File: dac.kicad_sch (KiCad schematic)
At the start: 10 parts, among them U11 TL074CDT, U12 MCP4728-E_UN

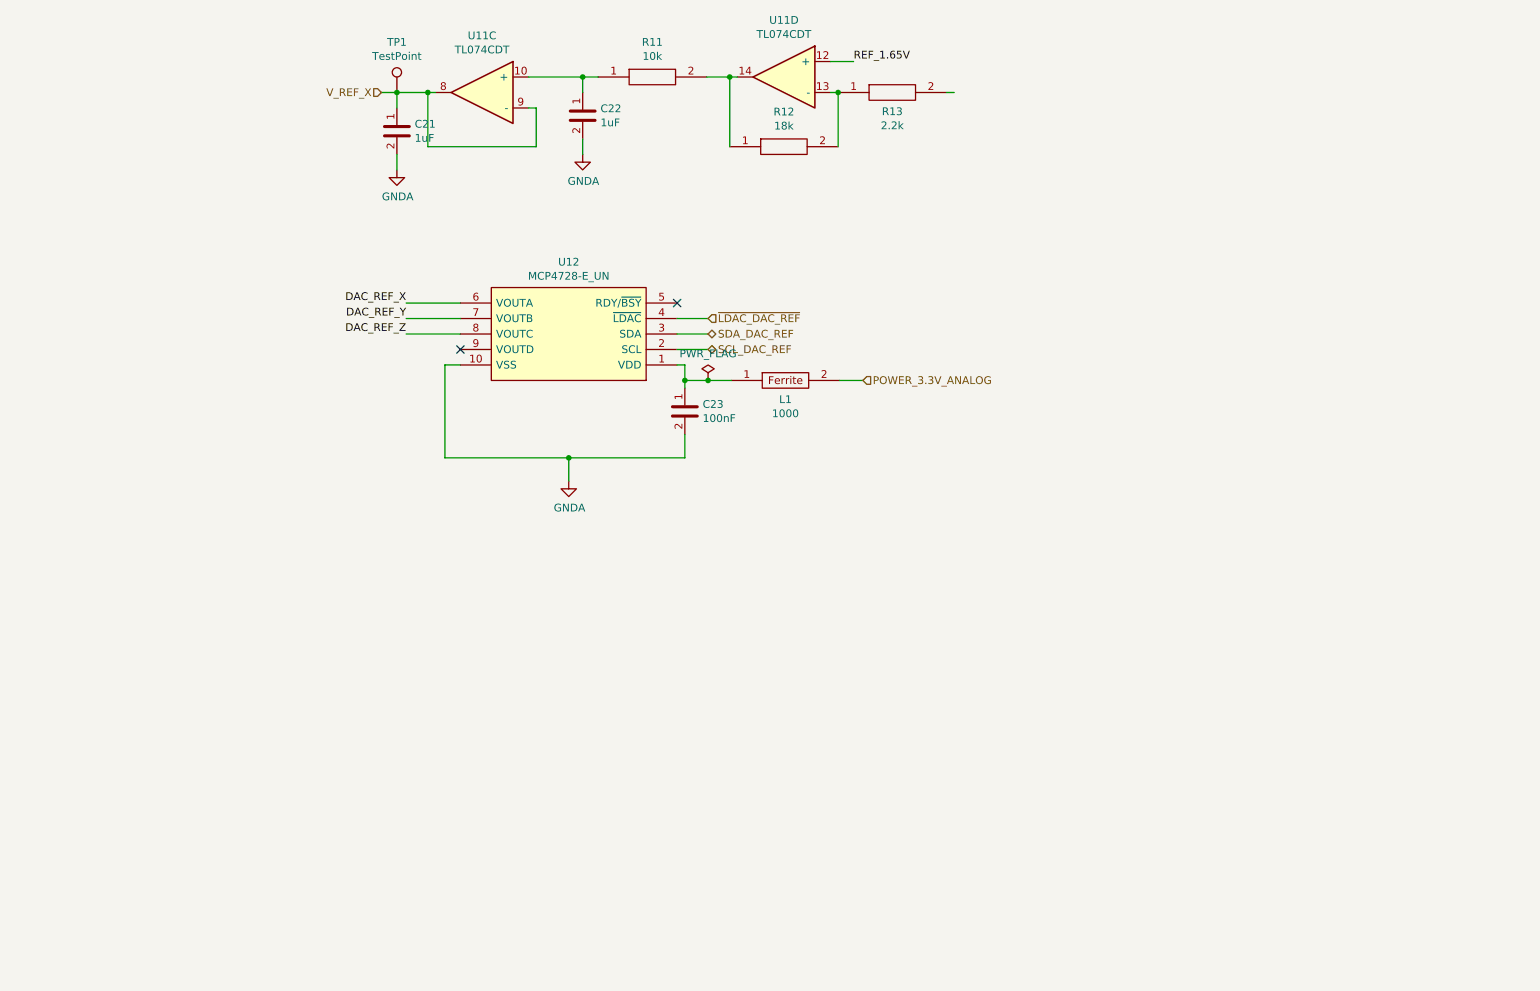
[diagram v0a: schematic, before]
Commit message: Added DAC circuit.
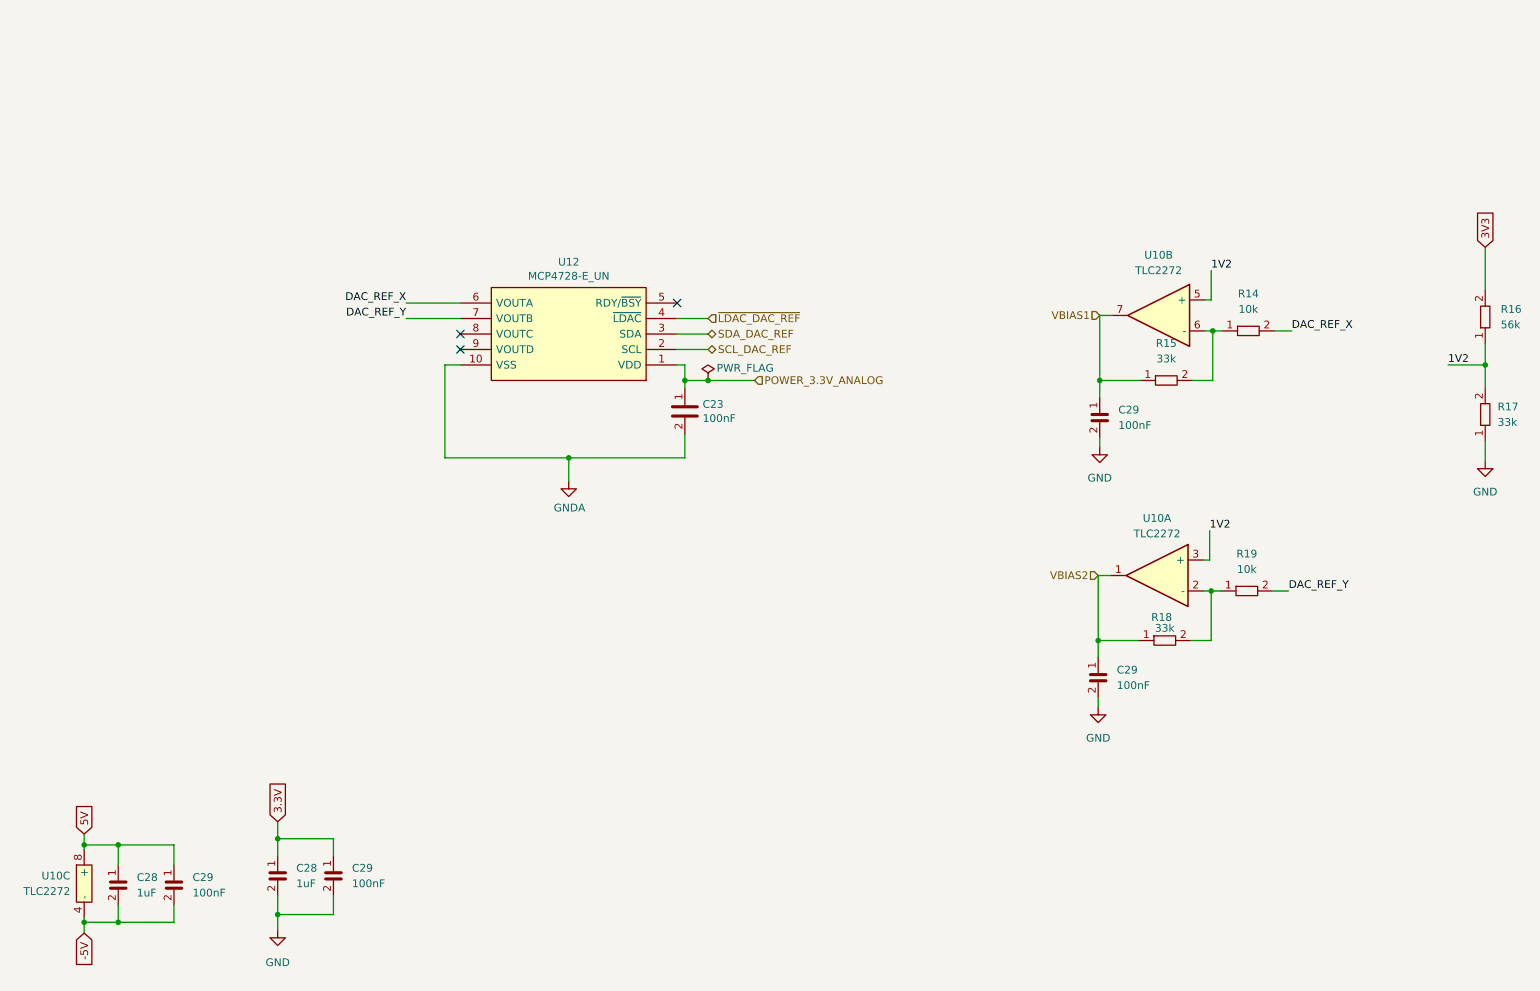
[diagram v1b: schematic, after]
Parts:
- removed C21, C22: C0603_1uF_25V, Capacitor_SMD:C_0603_1608Metric, symbol Basis_Platine_Kompass-rescue:C0603_1uF_25V-Jojo_Kicad_Lib
- removed L1: L0603_Ferrite_Bead_1k, Resistor_SMD:R_0603_1608Metric, symbol Basis_Platine_Kompass-rescue:L0603_Ferrite_Bead_1k-Jojo_Kicad_Lib
- removed R11: R0603_10k, Resistor_SMD:R_0603_1608Metric, symbol Basis_Platine_Kompass-rescue:R0603_10k-Jojo_Kicad_Lib
- removed R12: R0603_18k, Resistor_SMD:R_0603_1608Metric, symbol Basis_Platine_Kompass-rescue:R0603_18k-Jojo_Kicad_Lib
- removed R13: R0603_2.2k, Resistor_SMD:R_0603_1608Metric, symbol Basis_Platine_Kompass-rescue:R0603_2.2k-Jojo_Kicad_Lib
- removed TP1: TestPoint, TestPoint:TestPoint_Pad_D1.5mm, symbol Basis_Platine_Kompass-rescue:TestPoint-Jojo_Kicad_Lib
- removed U11: TL074CDT, SamacSys_Parts:SOIC127P600X175-14N, symbol Basis_Platine_Kompass-rescue:TL074CDT-Jojo_Kicad_Lib
- added C28 (x2): C0402_1uF_6.3V, Capacitor_SMD:C_0402_1005Metric, symbol Jojos_Lib:C0402_1uF_6.3V
- added C29 (x4): C0402_100nF_50V, Capacitor_SMD:C_0402_1005Metric, symbol Jojos_Lib:C0402_100nF_50V
- added R14, R19: R0402_10k, Resistor_SMD:R_0402_1005Metric, symbol Jojos_Lib:R0402_10k
- added R15, R17, R18: R0402_33k, Resistor_SMD:R_0402_1005Metric, symbol Jojos_Lib:R0402_33k
- added R16: R0402_56k, Resistor_SMD:R_0402_1005Metric, symbol Jojos_Lib:R0402_56k
- added U10: TLC2272, Package_SO:SO-8_3.9x4.9mm_P1.27mm, symbol Jojos_Lib:TLC2272CD
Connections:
- net DAC_REF_X: now also R14.2
- net DAC_REF_Y: now also R19.2
- net POWER_3.3V_ANALOG: now also C23.1, U12.1 (VDD)
- net DAC_REF_Z: no longer names the net of U12.8 (VOUTC)
- new net: R14.1, R15.2, U10.6 (-)
- new net: R18.2, R19.1, U10.2 (-)
- new net -5V: C28.2, C29.2, U10.4 (-)
- new net 1V2: R16.1, R17.2, U10.3 (+), U10.5 (+)
- new net 3.3V: C28.1, C29.1
- new net 3V3: R16.2
- new net 5V: C28.1, C29.1, U10.8 (+)
- new net GND: C28.2, C29.2, C29.2, C29.2, R17.1
- new net VBIAS1: C29.1, R15.1, U10.7
- new net VBIAS2: C29.1, R18.1, U10.1
- no-connect marks 2 -> 3

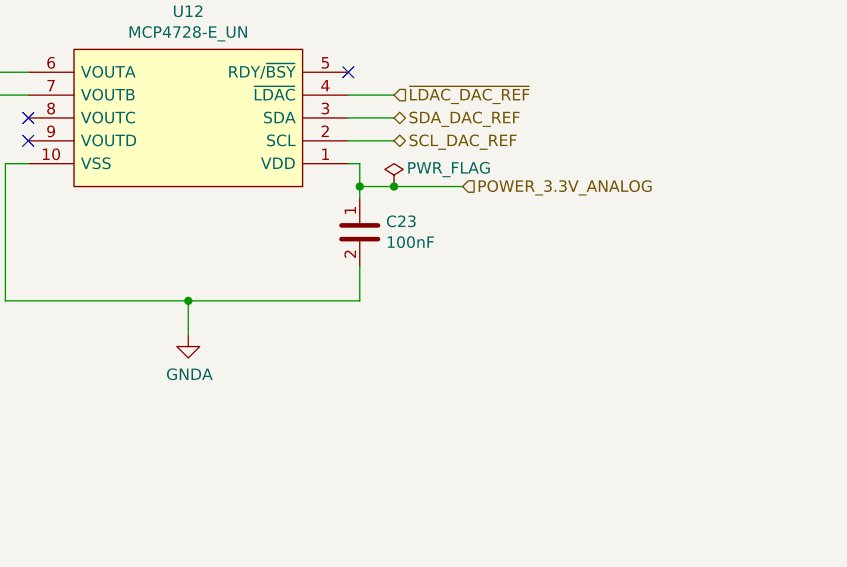
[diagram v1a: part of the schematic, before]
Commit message: Changed power supply.
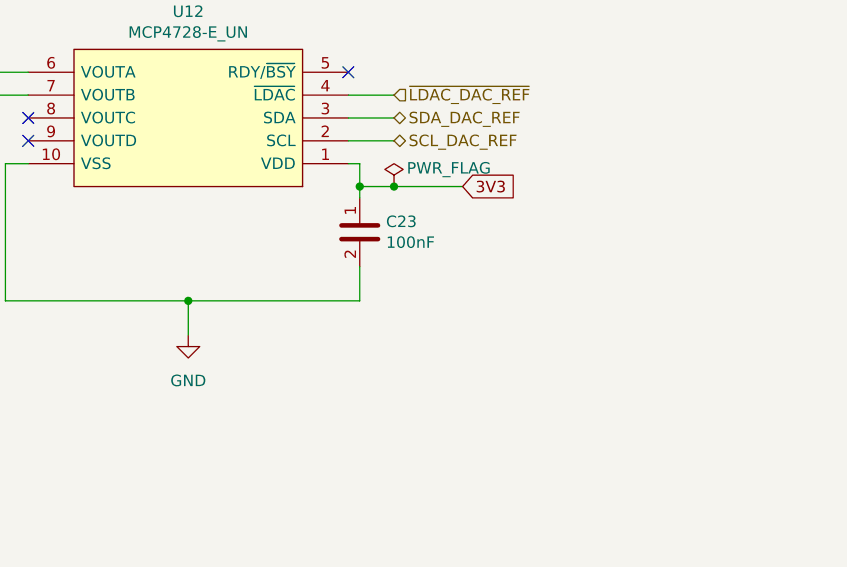
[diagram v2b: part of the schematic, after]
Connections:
- net GNDA is gone; now on net GND: C23.2, U12.10 (VSS)
- net POWER_3.3V_ANALOG is gone; now on net 3V3: C23.1, U12.1 (VDD)
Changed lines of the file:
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@@
+    )
+  )
+  (global_label "3V3" (shape input) (at 135.382 95.504 0) (fields_autoplaced)
+    (effects (font (size 1.27 1.27)) (justify left))
+    (property "Intersheetrefs" "${INTERSHEET_REFS}" (at 141.7954 95.504 0)
+      (effects (font (size 1.27 1.27)) (justify left) hide)
     )
   )
@@
   (hierarchical_label "VBIAS1" (shape input) (at 192.024 84.836 180) (fields_autoplaced)
     (effects (font (size 1.27 1.27)) (justify right))
-  )
-  (hierarchical_label "POWER_3.3V_ANALOG" (shape input) (at 135.382 95.504 0) (fields_autoplaced)
-    (effects (font (size 1.27 1.27)) (justify left))
   )
   (hierarchical_label "SDA_DAC_REF" (shape bidirectional) (at 127.762 87.884 0) (fields_autoplaced)
@@
     )
   )
-  (symbol (lib_id "power:GNDA") (at 104.902 112.014 0) (unit 1)
-    (in_bom yes) (on_board yes) (dnp no)
-    (property "Reference" "#PWR021" (at 104.902 118.364 0)
-      (effects (font (size 1.27 1.27)) hide)
-    )
-    (property "Value" "GNDA" (at 105.029 116.4082 0)
-      (effects (font (size 1.27 1.27)))
-    )
-    (property "Footprint" "" (at 104.902 112.014 0)
-      (effects (font (size 1.27 1.27)) hide)
-    )
-    (property "Datasheet" "" (at 104.902 112.014 0)
-      (effects (font (size 1.27 1.27)) hide)
-    )
-    (pin "1")
-    (instances
-      (project "CMEX"
-        (path "/03c4a148-37f4-4d5a-ada3-efb0d725ba7b"
-          (reference "#PWR021") (unit 1)
-        )
-        (path "/03c4a148-37f4-4d5a-ada3-efb0d725ba7b/4e3d1fe0-3870-440f-98d4-103735aef720"
-          (reference "#PWR020") (unit 1)
-        )
-      )
-      (project "Basis_Platine_Kompass"
-        (path "/8966b6e5-9901-4983-a621-a9b0fedaa794/00000000-0000-0000-0000-00005eadd7ff"
-          (reference "#PWR035") (unit 1)
-        )
-      )
-    )
-  )
   (symbol (lib_id "Jojos_Lib:TLC2272CD") (at 24.638 177.8 0) (unit 3)
     (in_bom yes) (on_board yes) (dnp no) (fields_autoplaced)
@@
         )
       )
+    )
+  )
+  (symbol (lib_id "power:GND") (at 104.902 112.014 0) (unit 1)
+    (in_bom yes) (on_board yes) (dnp no) (fields_autoplaced)
+    (property "Reference" "#PWR019" (at 104.902 118.364 0)
+      (effects (font (size 1.27 1.27)) hide)
+    )
+    (property "Value" "GND" (at 104.902 117.094 0)
+      (effects (font (size 1.27 1.27)))
+    )
+    (property "Footprint" "" (at 104.902 112.014 0)
+      (effects (font (size 1.27 1.27)) hide)
+    )
+    (property "Datasheet" "" (at 104.902 112.014 0)
+      (effects (font (size 1.27 1.27)) hide)
+    )
+    (pin "1")
+    (instances
+      (project "CMEX"
+        (path "/03c4a148-37f4-4d5a-ada3-efb0d725ba7b/4e3d1fe0-3870-440f-98d4-103735aef720"
+          (reference "#PWR019") (unit 1)
+        )
+      )

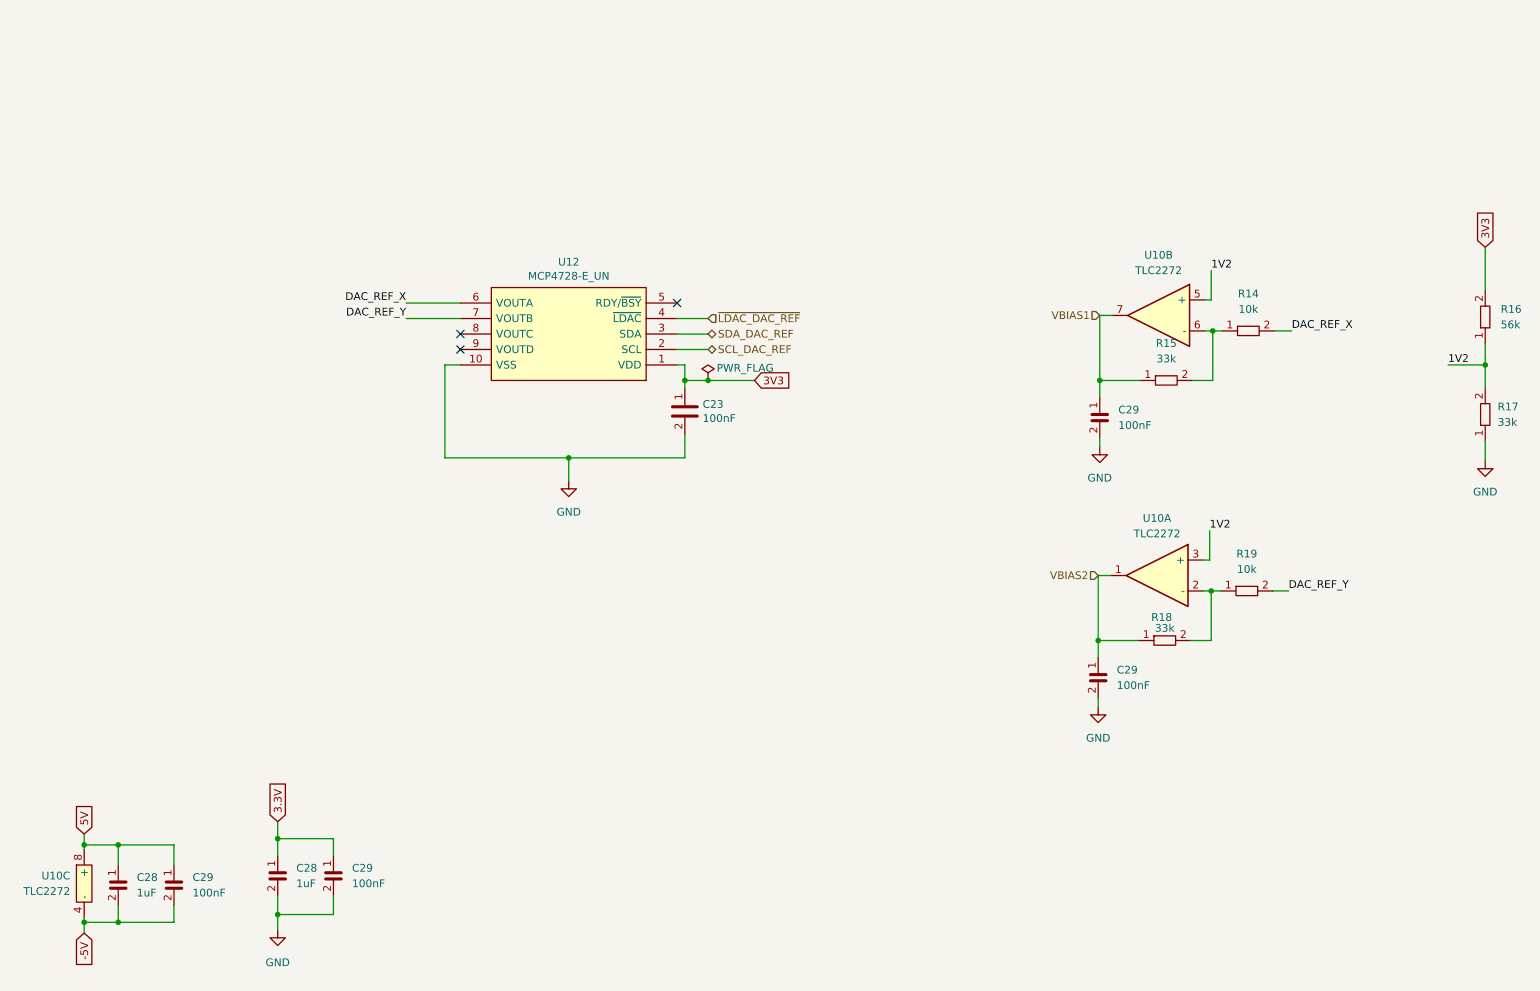
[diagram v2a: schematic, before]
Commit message: Changed global to hierarchichal lables, reorganized main sheet to get pins to connector.
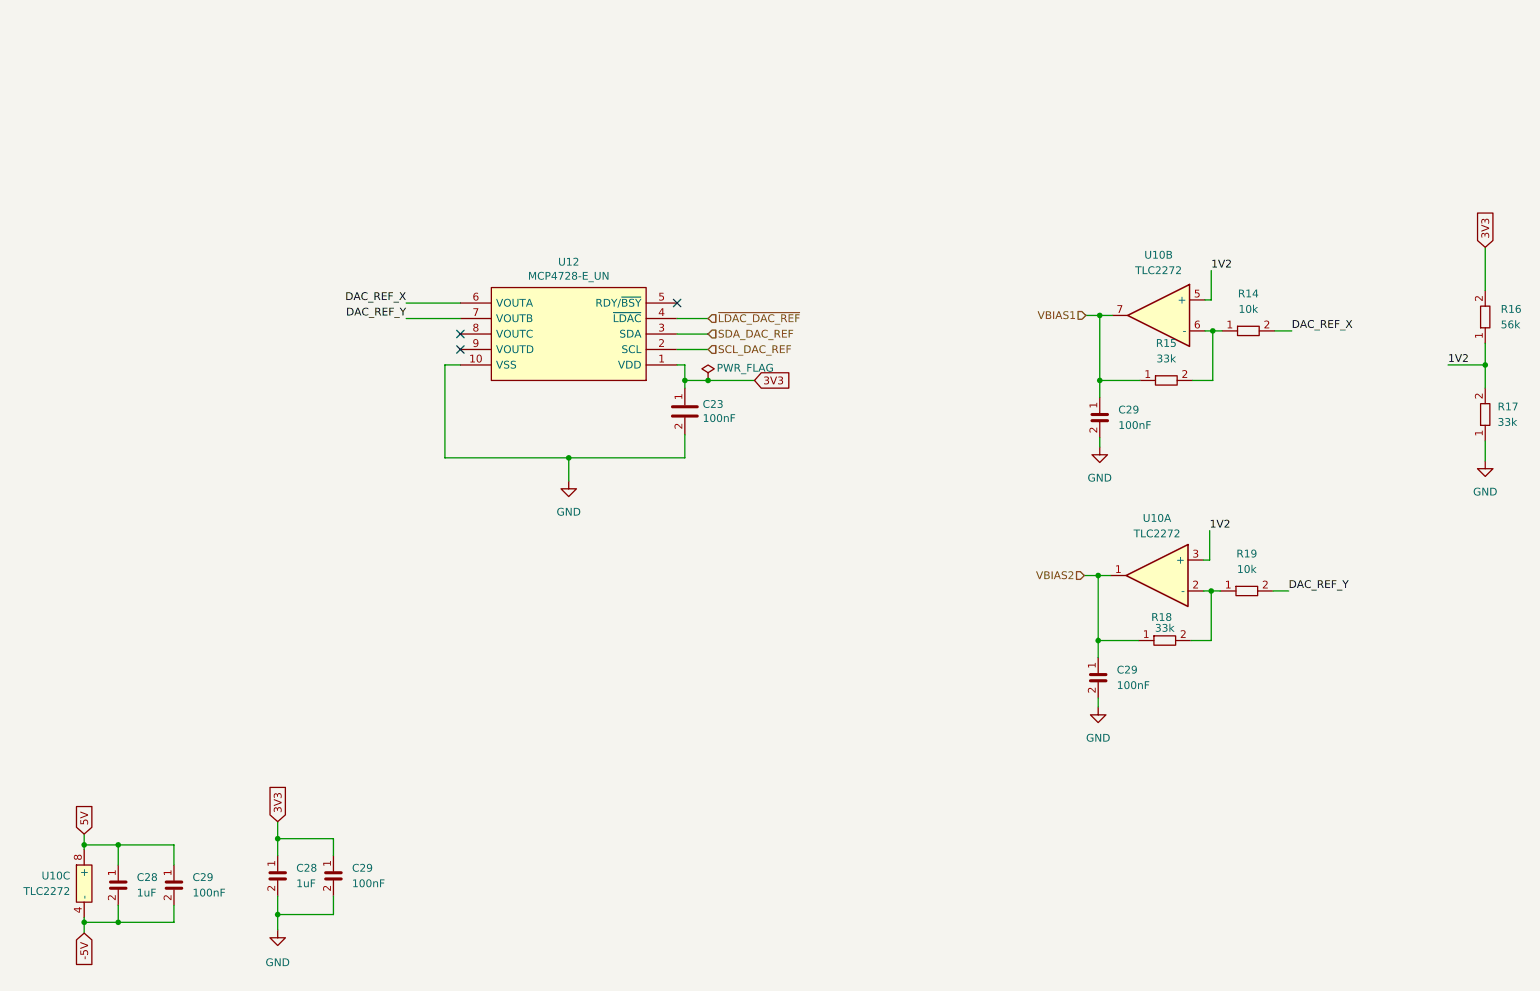
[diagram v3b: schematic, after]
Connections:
- net 3.3V is gone; now on net 3V3: C28.1, C29.1
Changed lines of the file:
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@@
   (junction (at 191.77 138.176) (diameter 0) (color 0 0 0 0)
   )
+  (junction (at 192.024 84.836) (diameter 0) (color 0 0 0 0)
+  )
   (junction (at 30.988 171.704) (diameter 0) (color 0 0 0 0)
   )
@@
   )
   (junction (at 30.988 184.404) (diameter 0) (color 0 0 0 0)
+  )
+  (junction (at 191.77 127.508) (diameter 0) (color 0 0 0 0)
   )
   (junction (at 210.312 130.048) (diameter 0) (color 0 0 0 0)
@@
     (stroke (width 0) (type default))
   )
+  (wire (pts (xy 189.738 84.836) (xy 192.024 84.836))
+    (stroke (width 0) (type default))
+  )
   (wire (pts (xy 209.296 82.296) (xy 210.312 82.296))
     (stroke (width 0) (type default))
@@
   )
   (wire (pts (xy 210.312 138.176) (xy 210.312 130.048))
+    (stroke (width 0) (type default))
+  )
+  (wire (pts (xy 189.484 127.508) (xy 191.77 127.508))
     (stroke (width 0) (type default))
   )
@@
     )
   )
-  (global_label "3.3V" (shape input) (at 57.15 167.894 90) (fields_autoplaced)
-    (effects (font (size 1.27 1.27)) (justify left))
-    (property "Intersheetrefs" "${INTERSHEET_REFS}" (at 57.15 160.8758 90)
+  (global_label "3V3" (shape input) (at 57.15 167.894 90) (fields_autoplaced)
+    (effects (font (size 1.27 1.27)) (justify left))
+    (property "Intersheetrefs" "${INTERSHEET_REFS}" (at 57.15 161.4806 90)
       (effects (font (size 1.27 1.27)) (justify left) hide)
     )
@@
     )
   )
-  (hierarchical_label "VBIAS2" (shape input) (at 191.77 127.508 180) (fields_autoplaced)
+  (hierarchical_label "VBIAS2" (shape input) (at 189.484 127.508 180) (fields_autoplaced)
     (effects (font (size 1.27 1.27)) (justify right))
   )
-  (hierarchical_label "SCL_DAC_REF" (shape bidirectional) (at 127.762 90.424 0) (fields_autoplaced)
+  (hierarchical_label "SCL_DAC_REF" (shape input) (at 127.762 90.424 0) (fields_autoplaced)
     (effects (font (size 1.27 1.27)) (justify left))
   )
@@
     (effects (font (size 1.27 1.27)) (justify left))
   )
-  (hierarchical_label "VBIAS1" (shape input) (at 192.024 84.836 180) (fields_autoplaced)
+  (hierarchical_label "VBIAS1" (shape input) (at 189.738 84.836 180) (fields_autoplaced)
     (effects (font (size 1.27 1.27)) (justify right))
   )
-  (hierarchical_label "SDA_DAC_REF" (shape bidirectional) (at 127.762 87.884 0) (fields_autoplaced)
-    (effects (font (size 1.27 1.27)) (justify left))
-  )
+  (hierarchical_label "SDA_DAC_REF" (shape input) (at 127.762 87.884 0) (fields_autoplaced)
+    (effects (font (size 1.27 1.27)) (justify left))
+  )
